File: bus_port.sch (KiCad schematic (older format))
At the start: 3 parts, among them P1 CONN_01X04, P1 CONN_01X40

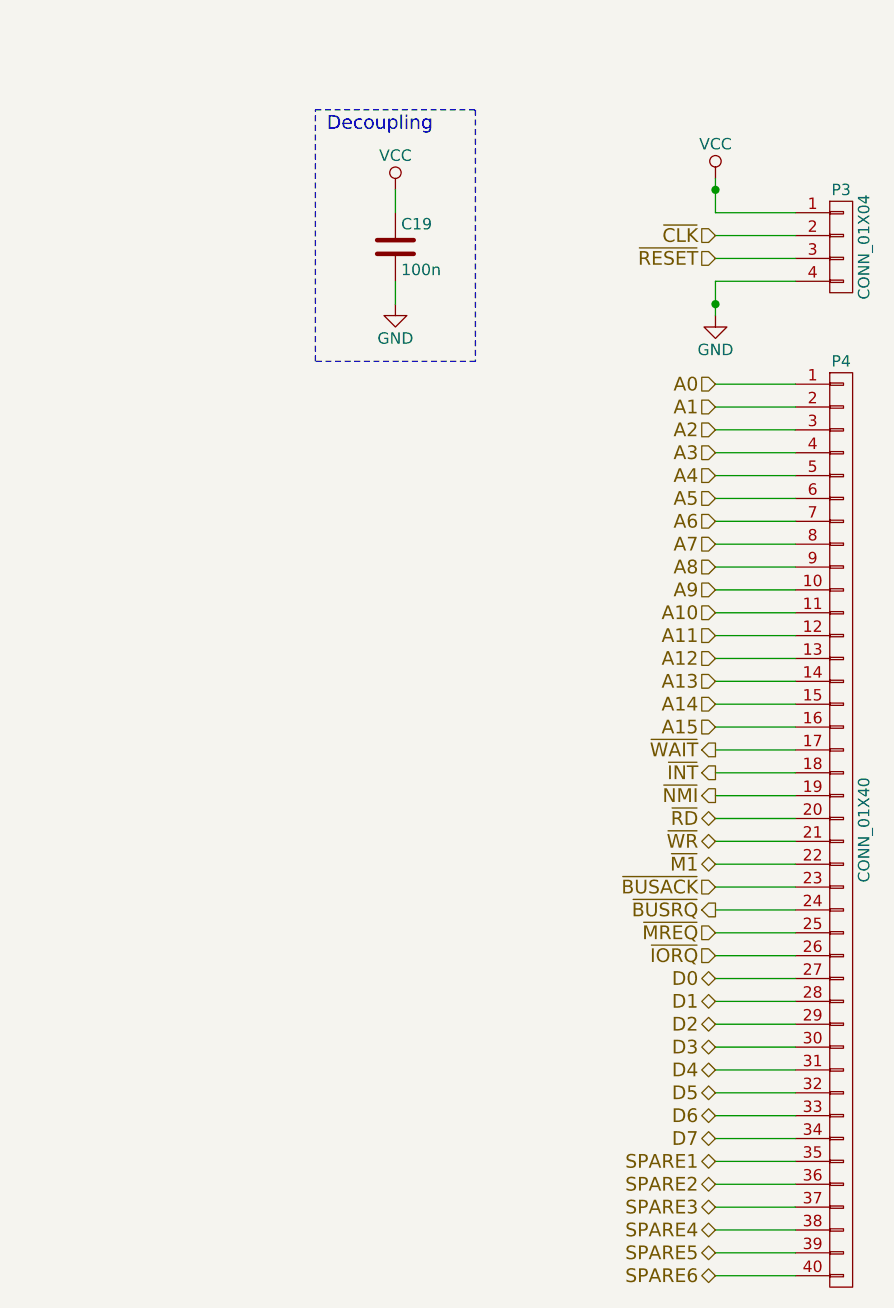
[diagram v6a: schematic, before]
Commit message: Added /intack signal and a pri-encoder for /iosel
Brain fart on the diode crap. Was tired. Added a priority encoder to
enable the Dx buffer so it properly tristates when no IObus ports are
selected.

Added a NOR gate to provide a /intack signal for any board to properly
detect their interupt has been accepted but the z80. Boards will need to
figure out who the interupt is for.

Will have to add interupt priority pins to the boards to allow the
boards to put jump vectors onto the data bus to service the interrupt
This should be fairly easy, just means the service pritority of the
slots will be A-H, with A being the highest priority and H being the
lowest.

Going to replace the hex inverters with the spare NOR gates too.
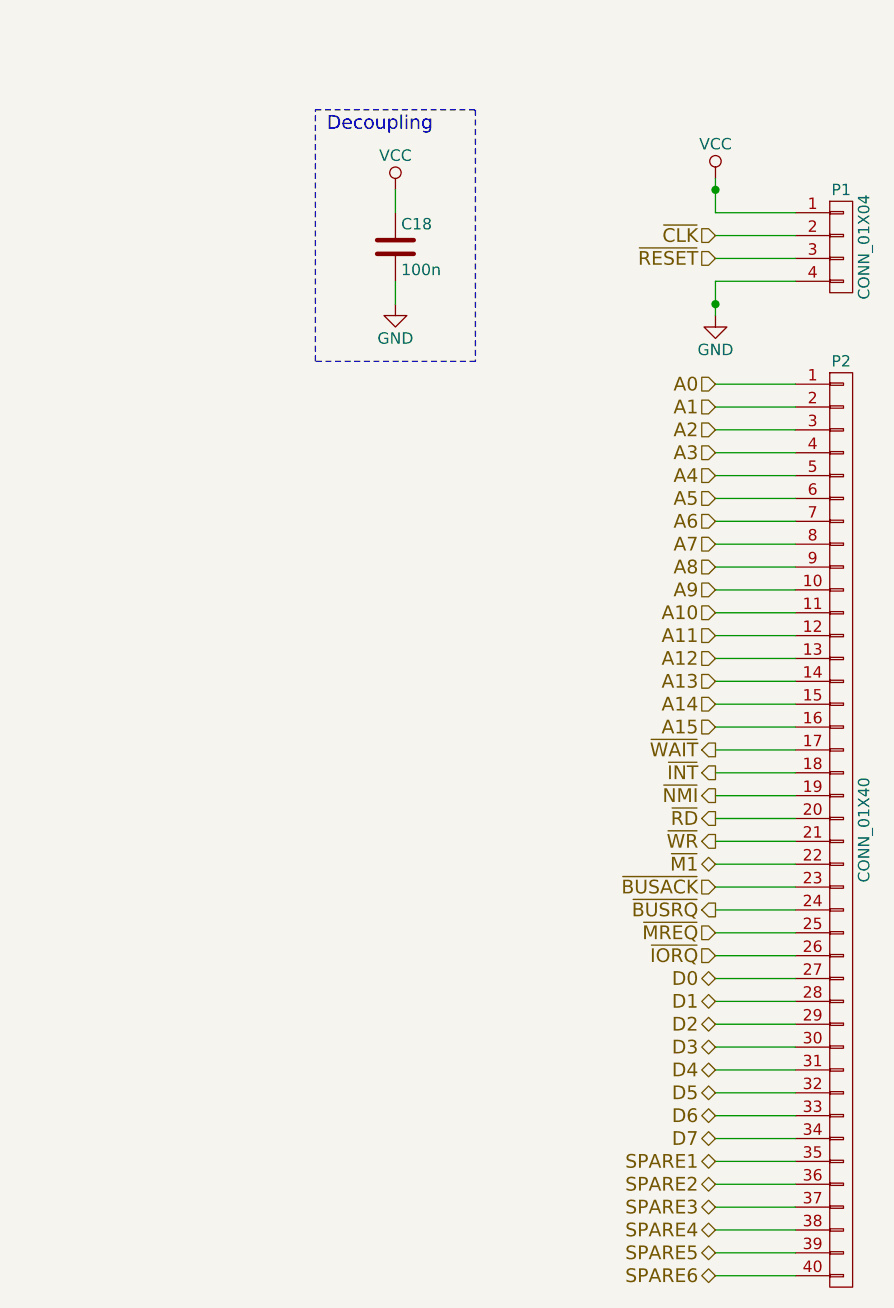
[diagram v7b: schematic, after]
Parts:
- C18: footprint (none) -> Capacitors_SMD:C_1206_HandSoldering
- P1: footprint (none) -> Pin_Headers:Pin_Header_Straight_1x04
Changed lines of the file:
@@
 $Descr A4 11693 8268
 encoding utf-8
-Sheet 4 16
+Sheet 13 14
 Title ""
 Date ""
@@
 Text HLabel 3900 4350 0    60   Output ~ 0
 ~INT
-Text HLabel 3900 4550 0    60   3State ~ 0
+Text HLabel 3900 4550 0    60   Output ~ 0
 ~RD
-Text HLabel 3900 4650 0    60   3State ~ 0
+Text HLabel 3900 4650 0    60   Output ~ 0
 ~WR
 Text HLabel 3900 4750 0    60   3State ~ 0
@@
 AR Path="/577F17CE/5783136E/577CEB68" Ref="P6"  Part="1"
 AR Path="/577F17CE/57832B70/577CEB68" Ref="P8"  Part="1"
-F 0 "P4" H 4450 6650 50  0000 C CNN
+F 0 "P2" H 4450 6650 50  0000 C CNN
 F 1 "CONN_01X40" V 4550 4600 50  0000 C CNN
 F 2 "Socket_Strips:Socket_Strip_Straight_1x40" H 4450 4600 50  0001 C CNN
@@
 AR Path="/577F17CE/5783136E/578144F7" Ref="P5"  Part="1"
 AR Path="/577F17CE/57832B70/578144F7" Ref="P7"  Part="1"
-F 0 "P3" H 4450 2300 50  0000 C CNN
+F 0 "P1" H 4450 2300 50  0000 C CNN
 F 1 "CONN_01X04" V 4550 2050 50  0000 C CNN
-F 2 "" H 4450 2050 50  0000 C CNN
+F 2 "Pin_Headers:Pin_Header_Straight_1x04" H 4450 2050 50  0001 C CNN
 F 3 "" H 4450 2050 50  0000 C CNN
 	1    4450 2050
@@
 	3900 1750 3900 1900
 $Comp
-L VCC #PWR17
+L VCC #PWR043
 U 1 1 5781454A
 P 3900 1750
-AR Path="/577F17CE/577F1897/5781454A" Ref="#PWR17"  Part="1"
+AR Path="/577F17CE/577F1897/5781454A" Ref="#PWR043"  Part="1"
 AR Path="/577F17CE/577F7EB3/5781454A" Ref="#PWR019"  Part="1"
 AR Path="/577F17CE/577F8AF5/5781454A" Ref="#PWR021"  Part="1"
 AR Path="/577F17CE/577F9440/5781454A" Ref="#PWR023"  Part="1"
-AR Path="/577F17CE/5782F6B6/5781454A" Ref="#PWR21"  Part="1"
-AR Path="/577F17CE/5783136E/5781454A" Ref="#PWR25"  Part="1"
-AR Path="/577F17CE/57832B70/5781454A" Ref="#PWR29"  Part="1"
-F 0 "#PWR21" H 3900 1600 50  0001 C CNN
+AR Path="/577F17CE/5782F6B6/5781454A" Ref="#PWR047"  Part="1"
+AR Path="/577F17CE/5783136E/5781454A" Ref="#PWR051"  Part="1"
+AR Path="/577F17CE/57832B70/5781454A" Ref="#PWR055"  Part="1"
+F 0 "#PWR055" H 3900 1600 50  0001 C CNN
 F 1 "VCC" H 3900 1900 50  0000 C CNN
 F 2 "" H 3900 1750 50  0000 C CNN
@@
 	3900 2200 3900 2350
 $Comp
-L GND #PWR18
+L GND #PWR044
 U 1 1 5781458A
 P 3900 2350
-AR Path="/577F17CE/577F1897/5781458A" Ref="#PWR18"  Part="1"
+AR Path="/577F17CE/577F1897/5781458A" Ref="#PWR044"  Part="1"
 AR Path="/577F17CE/577F7EB3/5781458A" Ref="#PWR020"  Part="1"
 AR Path="/577F17CE/577F8AF5/5781458A" Ref="#PWR022"  Part="1"
 AR Path="/577F17CE/577F9440/5781458A" Ref="#PWR024"  Part="1"
-AR Path="/577F17CE/5782F6B6/5781458A" Ref="#PWR22"  Part="1"
-AR Path="/577F17CE/5783136E/5781458A" Ref="#PWR26"  Part="1"
-AR Path="/577F17CE/57832B70/5781458A" Ref="#PWR30"  Part="1"
-F 0 "#PWR22" H 3900 2100 50  0001 C CNN
+AR Path="/577F17CE/5782F6B6/5781458A" Ref="#PWR048"  Part="1"
+AR Path="/577F17CE/5783136E/5781458A" Ref="#PWR052"  Part="1"
+AR Path="/577F17CE/57832B70/5781458A" Ref="#PWR056"  Part="1"
+F 0 "#PWR056" H 3900 2100 50  0001 C CNN
 F 1 "GND" H 3900 2200 50  0000 C CNN
 F 2 "" H 3900 2350 50  0000 C CNN
@@
 AR Path="/577F17CE/5783136E/5780CE22" Ref="C20"  Part="1"
 AR Path="/577F17CE/57832B70/5780CE22" Ref="C21"  Part="1"
-F 0 "C19" H 2525 2150 50  0000 L CNN
+F 0 "C18" H 2525 2150 50  0000 L CNN
 F 1 "100n" H 2525 1950 50  0000 L CNN
-F 2 "" H 2538 1900 50  0000 C CNN
+F 2 "Capacitors_SMD:C_1206_HandSoldering" H 2538 1900 50  0001 C CNN
 F 3 "" H 2500 2050 50  0000 C CNN
 	1    2500 2050
@@
 Connection ~ 3900 2300
 $Comp
-L VCC #PWR15
+L VCC #PWR045
 U 1 1 5780D6F2
 P 2500 1800
-AR Path="/577F17CE/577F1897/5780D6F2" Ref="#PWR15"  Part="1"
-AR Path="/577F17CE/5782F6B6/5780D6F2" Ref="#PWR19"  Part="1"
-AR Path="/577F17CE/5783136E/5780D6F2" Ref="#PWR23"  Part="1"
-AR Path="/577F17CE/57832B70/5780D6F2" Ref="#PWR27"  Part="1"
-F 0 "#PWR19" H 2500 1650 50  0001 C CNN
+AR Path="/577F17CE/577F1897/5780D6F2" Ref="#PWR045"  Part="1"
+AR Path="/577F17CE/5782F6B6/5780D6F2" Ref="#PWR049"  Part="1"
+AR Path="/577F17CE/5783136E/5780D6F2" Ref="#PWR053"  Part="1"
+AR Path="/577F17CE/57832B70/5780D6F2" Ref="#PWR057"  Part="1"
+F 0 "#PWR057" H 2500 1650 50  0001 C CNN
 F 1 "VCC" H 2500 1950 50  0000 C CNN
 F 2 "" H 2500 1800 50  0000 C CNN
@@
 $EndComp
 $Comp
-L GND #PWR16
+L GND #PWR046
 U 1 1 5780D706
 P 2500 2300
-AR Path="/577F17CE/577F1897/5780D706" Ref="#PWR16"  Part="1"
-AR Path="/577F17CE/5782F6B6/5780D706" Ref="#PWR20"  Part="1"
-AR Path="/577F17CE/5783136E/5780D706" Ref="#PWR24"  Part="1"
-AR Path="/577F17CE/57832B70/5780D706" Ref="#PWR28"  Part="1"
-F 0 "#PWR20" H 2500 2050 50  0001 C CNN
+AR Path="/577F17CE/577F1897/5780D706" Ref="#PWR046"  Part="1"
+AR Path="/577F17CE/5782F6B6/5780D706" Ref="#PWR050"  Part="1"
+AR Path="/577F17CE/5783136E/5780D706" Ref="#PWR054"  Part="1"
+AR Path="/577F17CE/57832B70/5780D706" Ref="#PWR058"  Part="1"
+F 0 "#PWR058" H 2500 2050 50  0001 C CNN
 F 1 "GND" H 2500 2150 50  0000 C CNN
 F 2 "" H 2500 2300 50  0000 C CNN
